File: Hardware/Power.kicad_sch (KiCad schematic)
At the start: 30 parts, among them J2 JST_2mm_LiPo, Q2 SIL2308, U10 MCP73833_MSOP, U11 AP2112K-3.3, U12 STLQ015-3.3, U4 MAX17048, U5 AP2112K-3.3

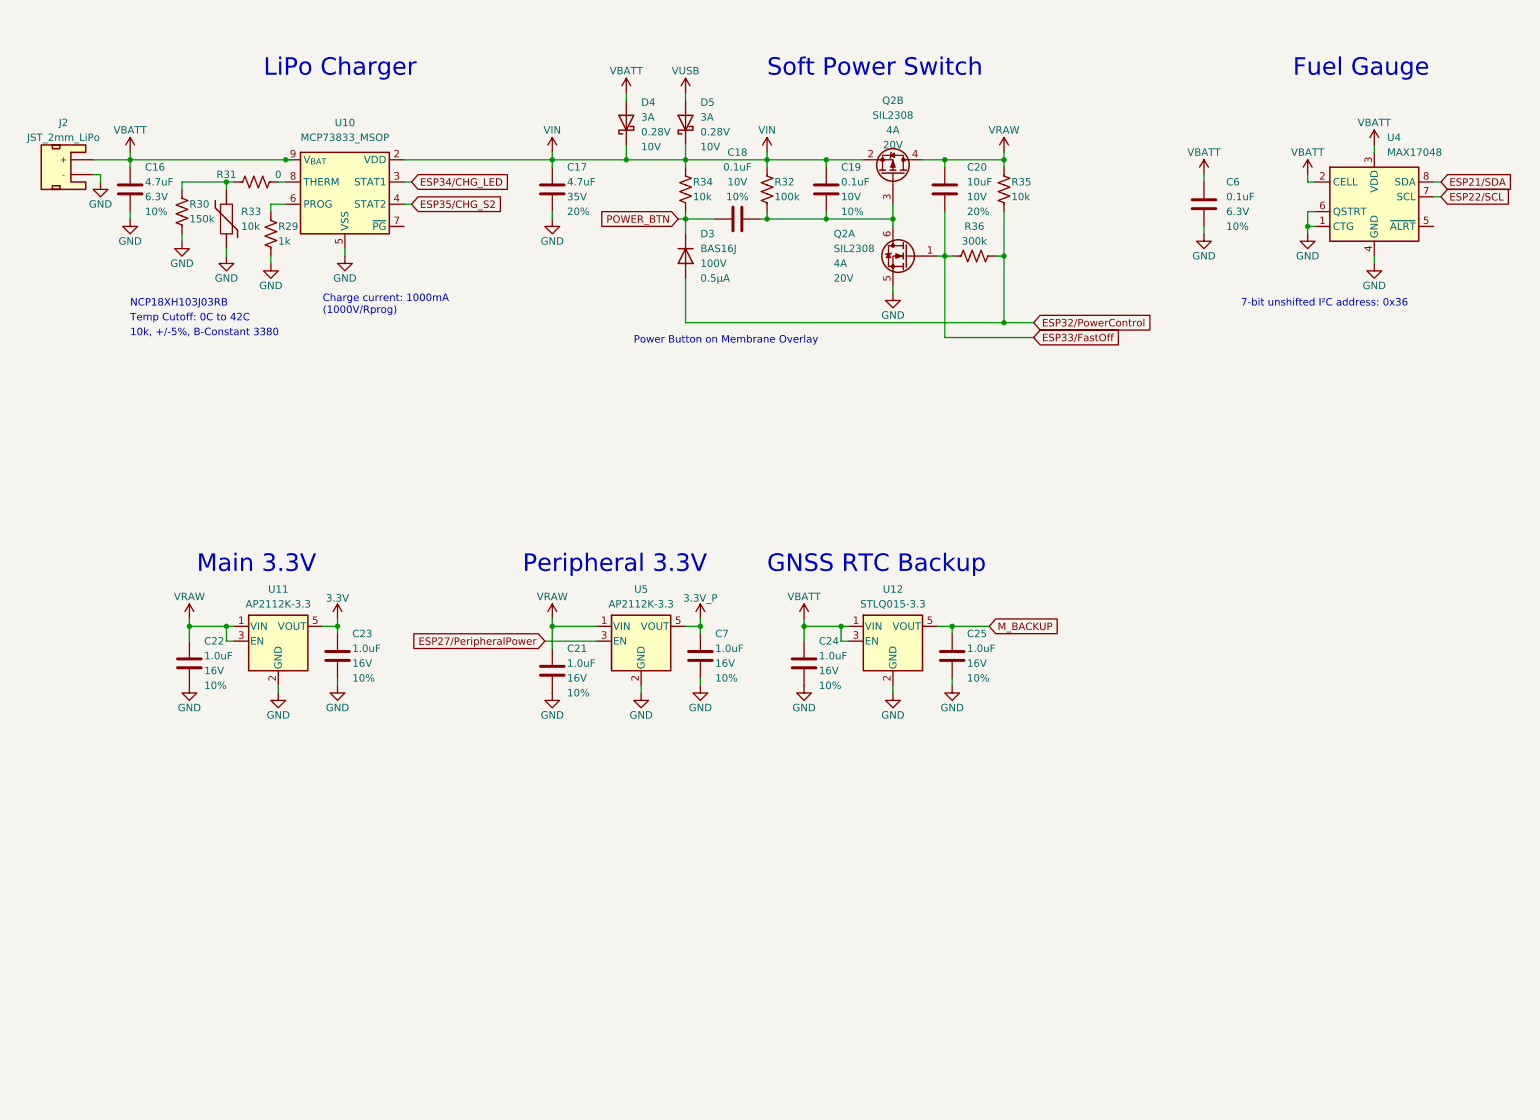
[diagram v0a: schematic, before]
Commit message: Schematic updates
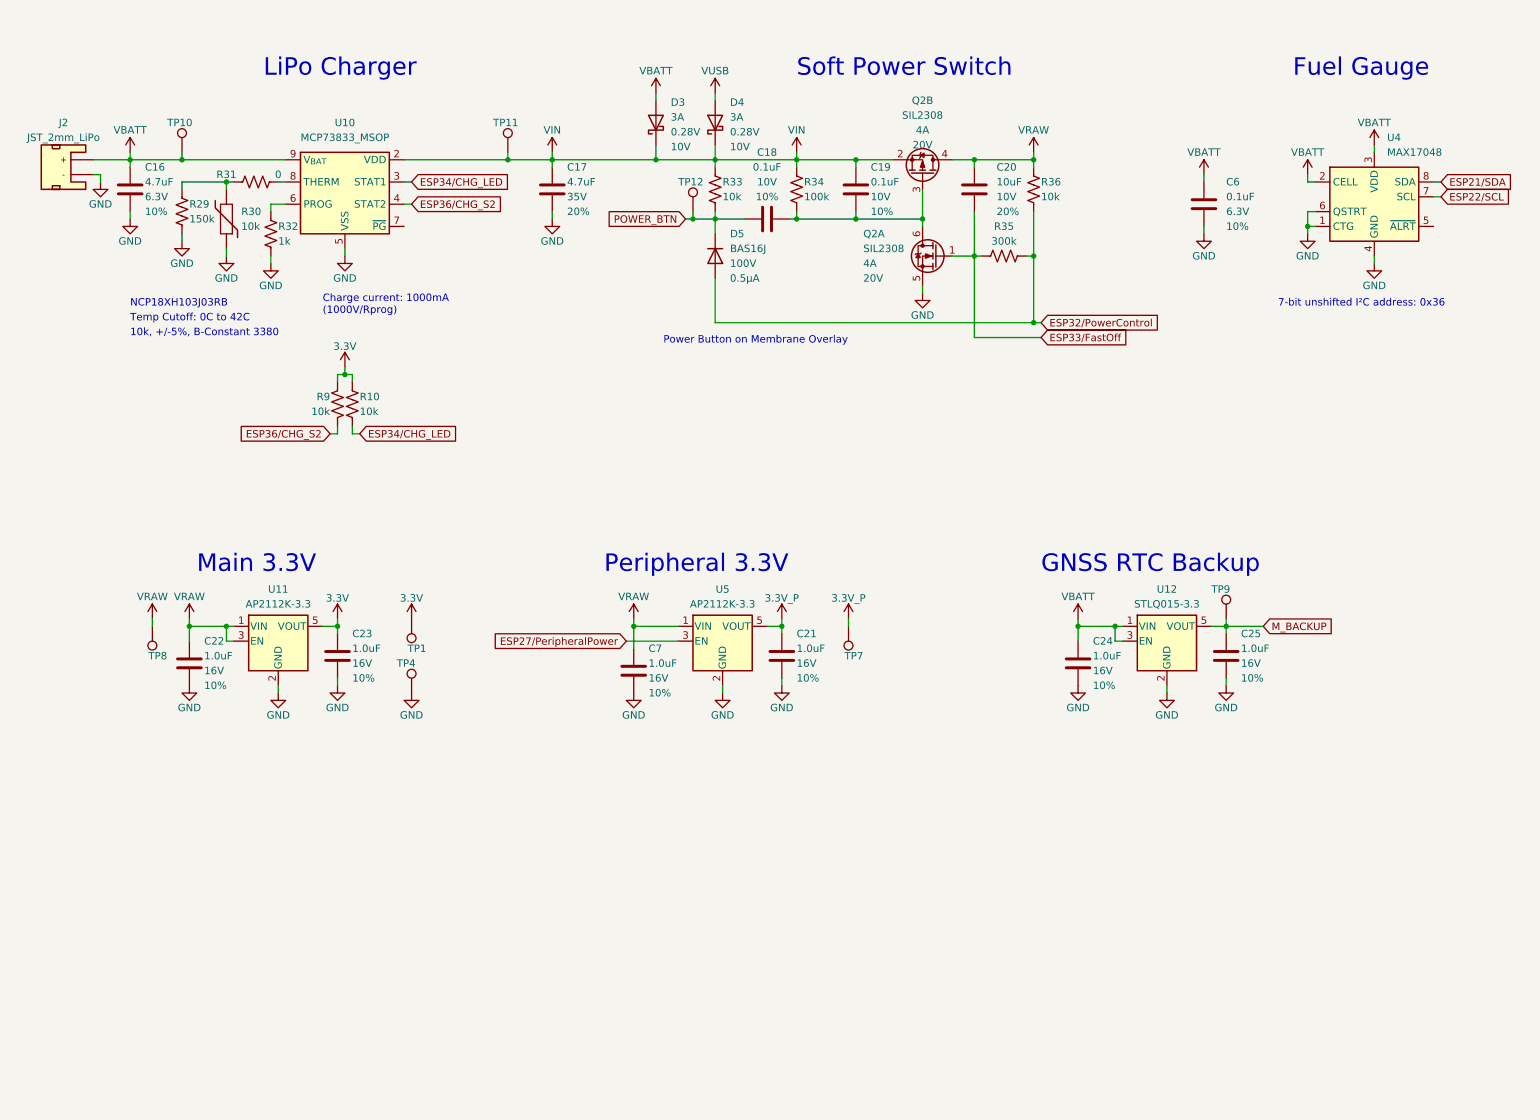
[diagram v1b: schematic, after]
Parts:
- added R10, R9: 10k, SparkFun-Resistor:R_0402_1005Metric, symbol SparkFun-Resistor:10k_0402
- added TP1, TP10, TP11, TP12, TP4, TP7, TP8, TP9: PTH, SparkFun-Connector:1X01, symbol SparkFun-Connector:TestPoint_PTH
- renumbered C7 to C21, C21 to C7, D4 to D3, D5 to D4, D3 to D5, R30 to R29, R33 to R30, R29 to R32, R34 to R33, R32 to R34, R36 to R35, R35 to R36
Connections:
- net 3.3V: now also R10.1, R9.1, TP1.1
- net 3.3V_P: now also TP7.1
- net ESP34/CHG_LED: now also R10.2
- net GND: now also U4.9 (GND), TP4.1
- net M_BACKUP: now also TP9.1
- net POWER_BTN: now also TP12.1
- net VBATT: now also TP10.1
- net VDD: now also TP11.1
- net VRAW: now also TP8.1
- net ESP35/CHG_S2 renamed ESP36/CHG_S2
- net ESP36/CHG_S2: now also R9.2
- new net: J2.NC1, J2.NC2
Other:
- moved on the sheet: C18, C19, C20, C21, C24, C25, C7, D3, D4, D5, R33, R34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

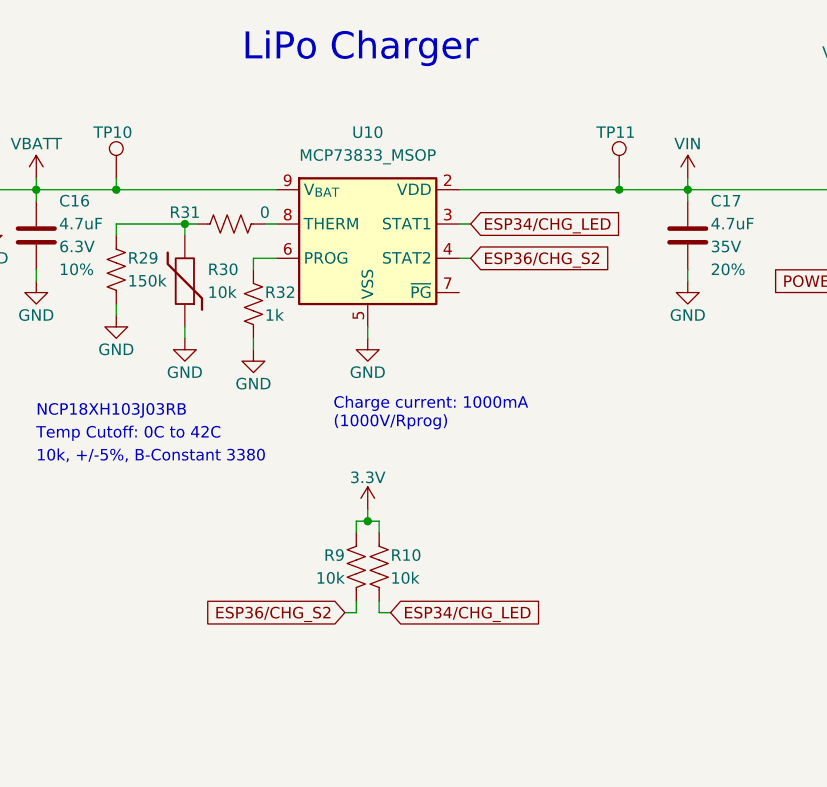
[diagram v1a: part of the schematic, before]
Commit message: Ready for airwire review
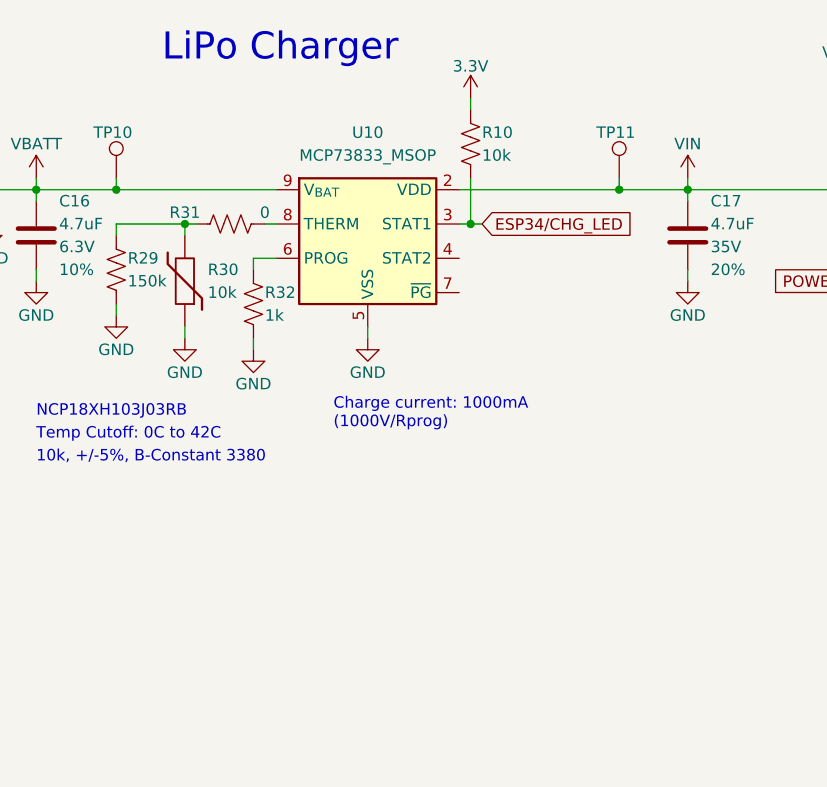
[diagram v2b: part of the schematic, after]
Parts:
- removed R9: 10k, SparkFun-Resistor:R_0402_1005Metric, symbol SparkFun-Resistor:10k_0402
- Q2: PROD_ID (none) -> TRANS-15717
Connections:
- net ESP36/CHG_S2: no longer names the net of U10.4 (STAT2)
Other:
- moved on the sheet: R10
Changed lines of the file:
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@@
   (junction (at 97.79 38.1) (diameter 0) (color 0 0 0 0)
   )
+  (junction (at 81.28 41.91) (diameter 0) (color 0 0 0 0)
+  )
   (junction (at 68.58 118.11) (diameter 0) (color 0 0 0 0)
   )
@@
   (junction (at 168.91 48.26) (diameter 0) (color 0 0 0 0)
   )
-  (junction (at 69.85 74.93) (diameter 0) (color 0 0 0 0)
-  )
   (junction (at 129.54 48.26) (diameter 0) (color 0 0 0 0)
   )
@@
     (stroke (width 0) (type default))
   )
-  (wire (pts (xy 68.58 76.2) (xy 68.58 74.93))
-    (stroke (width 0) (type default))
-  )
   (wire (pts (xy 256.54 41.91) (xy 257.81 41.91))
     (stroke (width 0) (type default))
@@
     (stroke (width 0) (type default))
   )
-  (wire (pts (xy 71.12 85.09) (xy 72.39 85.09))
-    (stroke (width 0) (type default))
-  )
   (wire (pts (xy 27.94 40.64) (xy 27.94 41.91))
     (stroke (width 0) (type default))
@@
     (stroke (width 0) (type default))
   )
+  (wire (pts (xy 81.28 41.91) (xy 82.55 41.91))
+    (stroke (width 0) (type default))
+  )
   (wire (pts (xy 66.04 118.11) (xy 68.58 118.11))
     (stroke (width 0) (type default))
@@
     (stroke (width 0) (type default))
   )
+  (wire (pts (xy 81.28 36.83) (xy 81.28 41.91))
+    (stroke (width 0) (type default))
+  )
   (wire (pts (xy 168.91 60.96) (xy 168.91 59.69))
     (stroke (width 0) (type default))
   )
-  (wire (pts (xy 68.58 83.82) (xy 68.58 85.09))
-    (stroke (width 0) (type default))
-  )
   (wire (pts (xy 43.18 118.11) (xy 43.18 120.65))
     (stroke (width 0) (type default))
@@
     (stroke (width 0) (type default))
   )
-  (wire (pts (xy 69.85 73.66) (xy 69.85 74.93))
-    (stroke (width 0) (type default))
-  )
   (wire (pts (xy 234.95 46.99) (xy 234.95 49.53))
     (stroke (width 0) (type default))
@@
     (stroke (width 0) (type default))
   )
-  (wire (pts (xy 69.85 74.93) (xy 71.12 74.93))
-    (stroke (width 0) (type default))
-  )
   (wire (pts (xy 33.02 36.83) (xy 33.02 38.1))
     (stroke (width 0) (type default))
@@
     (stroke (width 0) (type default))
   )
-  (wire (pts (xy 68.58 74.93) (xy 69.85 74.93))
-    (stroke (width 0) (type default))
-  )
   (wire (pts (xy 177.8 68.58) (xy 189.23 68.58))
     (stroke (width 0) (type default))
@@
     (stroke (width 0) (type default))
   )
-  (wire (pts (xy 68.58 85.09) (xy 67.31 85.09))
-    (stroke (width 0) (type default))
-  )
   (wire (pts (xy 146.05 48.26) (xy 147.32 48.26))
     (stroke (width 0) (type default))
@@
     (stroke (width 0) (type default))
   )
-  (wire (pts (xy 71.12 83.82) (xy 71.12 85.09))
-    (stroke (width 0) (type default))
-  )
   (wire (pts (xy 128.27 48.26) (xy 129.54 48.26))
     (stroke (width 0) (type default))
@@
     (stroke (width 0) (type default))
   )
-  (wire (pts (xy 71.12 76.2) (xy 71.12 74.93))
+  (wire (pts (xy 81.28 27.94) (xy 81.28 29.21))
     (stroke (width 0) (type default))
   )
@@
   )
   (wire (pts (xy 187.96 66.04) (xy 189.23 66.04))
-    (stroke (width 0) (type default))
-  )
-  (wire (pts (xy 80.01 45.72) (xy 81.28 45.72))
     (stroke (width 0) (type default))
   )
@@
     (effects (font (size 3 3)) (justify left bottom))
   )
-  (text "LiPo Charger" (at 55.88 24.13 0)
+  (text "LiPo Charger" (at 46.99 24.13 0)
     (effects (font (size 3 3)) (justify left bottom))
   )
@@
   (text "7-bit unshifted I²C address: 0x36\n" (at 229.87 63.5 0)
     (effects (font (size 1.27 1.27)) (justify left bottom))
-  )
-  (global_label "ESP36{slash}CHG_S2" (shape input) (at 67.31 85.09 180) (fields_autoplaced)
-    (effects (font (size 1.27 1.27)) (justify right))
-    (property "Intersheetrefs" "${INTERSHEET_REFS}" (at 49.6897 85.09 0)
-      (effects (font (size 1.27 1.27)) (justify right) hide)
-    )
   )
   (global_label "ESP21{slash}SDA" (shape input) (at 257.81 41.91 0) (fields_autoplaced)
@@
     )
   )
-  (global_label "ESP34{slash}CHG_LED" (shape input) (at 81.28 41.91 0) (fields_autoplaced)
+  (global_label "ESP34{slash}CHG_LED" (shape input) (at 82.55 41.91 0) (fields_autoplaced)
     (effects (font (size 1.27 1.27)) (justify left))
-    (property "Intersheetrefs" "${INTERSHEET_REFS}" (at 99.9284 41.91 0)
+    (property "Intersheetrefs" "${INTERSHEET_REFS}" (at 101.1984 41.91 0)
       (effects (font (size 1.27 1.27)) (justify left) hide)
     )
@@
     (effects (font (size 1.27 1.27)) (justify left))
     (property "Intersheetrefs" "${INTERSHEET_REFS}" (at 271.6808 44.45 0)
-      (effects (font (size 1.27 1.27)) (justify left) hide)
-    )
-  )
-  (global_label "ESP36{slash}CHG_S2" (shape input) (at 81.28 45.72 0) (fields_autoplaced)
-    (effects (font (size 1.27 1.27)) (justify left))
-    (property "Intersheetrefs" "${INTERSHEET_REFS}" (at 98.9003 45.72 0)
-      (effects (font (size 1.27 1.27)) (justify left) hide)
-    )
-  )
-  (global_label "ESP34{slash}CHG_LED" (shape input) (at 72.39 85.09 0) (fields_autoplaced)
-    (effects (font (size 1.27 1.27)) (justify left))
-    (property "Intersheetrefs" "${INTERSHEET_REFS}" (at 91.0384 85.09 0)
       (effects (font (size 1.27 1.27)) (justify left) hide)
     )
@@
     )
   )
-  (symbol (lib_id "SparkFun-Resistor:10k_0402") (at 68.58 80.01 270) (mirror x) (unit 1)
-    (in_bom yes) (on_board yes) (dnp no)
-    (property "Reference" "R9" (at 67.31 78.74 90)
-      (effects (font (size 1.27 1.27)) (justify right))
-    )
-    (property "Value" "10k" (at 67.31 81.28 90)
-      (effects (font (size 1.27 1.27)) (justify right))
-    )
-    (property "Footprint" "SparkFun-Resistor:R_0402_1005Metric" (at 64.516 80.01 0)
-      (effects (font (size 1.27 1.27)) hide)
-    )
-    (property "Datasheet" "https://www.vishay.com/docs/20035/dcrcwe3.pdf" (at 60.96 80.01 0)
-      (effects (font (size 1.27 1.27)) hide)
-    )
-    (property "PROD_ID" "RES-14241" (at 62.484 80.01 0)
-      (effects (font (size 1.27 1.27)) hide)
-    )
-    (pin "1")
-    (pin "2")
-    (instances
-      (project "SparkFun_RTK_Facet_mosaic"
-        (path "/e3dd3ae4-244d-4cba-9cca-5d2abf83f29a/476b4701-5340-4853-910a-2af933cad777"
-          (reference "R9") (unit 1)
-        )
-      )
-    )
-  )
   (symbol (lib_id "power:GND") (at 49.53 54.61 0) (unit 1)
     (in_bom yes) (on_board yes) (dnp no)
@@
       (effects (font (size 1.27 1.27)) hide)
     )
-    (property "PROD_ID" "~" (at 154.94 40.64 0)
+    (property "PROD_ID" "TRANS-15717" (at 154.94 40.64 0)
       (effects (font (size 1.27 1.27)) hide)
     )
@@
       (effects (font (size 1.27 1.27)) hide)
     )
-    (property "PROD_ID" "~" (at 171.45 68.58 0)
+    (property "PROD_ID" "TRANS-15717" (at 171.45 68.58 0)
       (effects (font (size 1.27 1.27)) hide)
     )
@@
     )
   )
-  (symbol (lib_id "SparkFun-PowerSymbol:3.3V") (at 69.85 73.66 0) (unit 1)
-    (in_bom yes) (on_board yes) (dnp no)
-    (property "Reference" "#PWR0112" (at 69.85 77.47 0)
-      (effects (font (size 1.27 1.27)) hide)
-    )
-    (property "Value" "3.3V" (at 69.85 70.104 0)
-      (effects (font (size 1.27 1.27)))
-    )
-    (property "Footprint" "" (at 69.85 73.66 0)
-      (effects (font (size 1.27 1.27)) hide)
-    )
-    (property "Datasheet" "" (at 69.85 73.66 0)
+  (symbol (lib_id "SparkFun-PowerSymbol:3.3V") (at 81.28 27.94 0) (unit 1)
+    (in_bom yes) (on_board yes) (dnp no)
+    (property "Reference" "#PWR0112" (at 81.28 31.75 0)
+      (effects (font (size 1.27 1.27)) hide)
+    )
+    (property "Value" "3.3V" (at 81.28 24.384 0)
+      (effects (font (size 1.27 1.27)))
+    )
+    (property "Footprint" "" (at 81.28 27.94 0)
+      (effects (font (size 1.27 1.27)) hide)
+    )
+    (property "Datasheet" "" (at 81.28 27.94 0)
       (effects (font (size 1.27 1.27)) hide)
     )
@@
     )
   )
-  (symbol (lib_id "SparkFun-Resistor:10k_0402") (at 71.12 80.01 90) (unit 1)
-    (in_bom yes) (on_board yes) (dnp no)
-    (property "Reference" "R10" (at 72.39 78.74 90)
-      (effects (font (size 1.27 1.27)) (justify right))
-    )
-    (property "Value" "10k" (at 72.39 81.28 90)
-      (effects (font (size 1.27 1.27)) (justify right))
-    )
-    (property "Footprint" "SparkFun-Resistor:R_0402_1005Metric" (at 75.184 80.01 0)
-      (effects (font (size 1.27 1.27)) hide)
-    )
-    (property "Datasheet" "https://www.vishay.com/docs/20035/dcrcwe3.pdf" (at 78.74 80.01 0)
-      (effects (font (size 1.27 1.27)) hide)
-    )
-    (property "PROD_ID" "RES-14241" (at 77.216 80.01 0)
-      (effects (font (size 1.27 1.27)) hide)
-    )
+  (symbol (lib_id "SparkFun-Resistor:10k_0402") (at 81.28 33.02 90) (unit 1)
+    (in_bom yes) (on_board yes) (dnp no)
+    (property "Reference" "R10" (at 82.55 31.75 90)
+      (effects (font (size 1.27 1.27)) (justify right))
+    )
+    (property "Value" "10k" (at 82.55 34.29 90)
+      (effects (font (size 1.27 1.27)) (justify right))
+    )
+    (property "Footprint" "SparkFun-Resistor:R_0402_1005Metric" (at 85.344 33.02 0)
+      (effects (font (size 1.27 1.27)) hide)
+    )
+    (property "Datasheet" "https://www.vishay.com/docs/20035/dcrcwe3.pdf" (at 88.9 33.02 0)
+      (effects (font (size 1.27 1.27)) hide)
+    )
+    (property "PROD_ID" "RES-14241" (at 87.376 33.02 0)
+      (effects (font (size 1.27 1.27)) hide)
+    )

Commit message: Do over with RSP32 Pico Mini - routed
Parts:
- added R9: 10k, SparkFun-Resistor:R_0402_1005Metric, symbol SparkFun-Resistor:10k_0402
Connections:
- net 3.3V: now also R9.1
- net ESP37/CHG_STAT2: now reaches U10.4 (STAT2)
- net ESP37/CHG_STAT2: now also R9.2
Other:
- moved on the sheet: C17, R10, TP11

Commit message: Switching back to the WROVER - routed
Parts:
- removed R9: 10k, SparkFun-Resistor:R_0402_1005Metric, symbol SparkFun-Resistor:10k_0402
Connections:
- net ESP37/CHG_STAT2: no longer names the net of U10.4 (STAT2)
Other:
- moved on the sheet: C17, R10, TP11

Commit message: Add extra Test Points
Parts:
- added TP23: PTH, SparkFun-Connector:1X01, symbol SparkFun-Connector:TestPoint_PTH
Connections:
- net GND: now also TP23.1
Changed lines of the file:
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@@
+    )
+  )
+  (symbol (lib_id "SparkFun-Connector:TestPoint_PTH") (at 86.36 129.54 0) (unit 1)
+    (in_bom yes) (on_board yes) (dnp no)
+    (property "Reference" "TP23" (at 83.82 124.46 0)
+      (effects (font (size 1.27 1.27)) (justify left))
+    )
+    (property "Value" "PTH" (at 86.36 133.35 0)
+      (effects (font (size 1.27 1.27)) hide)
+    )
+    (property "Footprint" "SparkFun-Connector:1X01" (at 85.09 135.89 0)
+      (effects (font (size 1.27 1.27)) hide)
+    )
+    (property "Datasheet" "~" (at 86.36 137.16 0)
+      (effects (font (size 1.27 1.27)) hide)
+    )
+    (pin "1")
+    (instances
+      (project "SparkFun_RTK_Facet_mosaic"
+        (path "/e3dd3ae4-244d-4cba-9cca-5d2abf83f29a/476b4701-5340-4853-910a-2af933cad777"
+          (reference "TP23") (unit 1)
+        )
+      )
     )
   )
@@
         )
       )
+    )
+  )
+  (symbol (lib_id "SparkFun-PowerSymbol:GND") (at 86.36 129.54 0) (unit 1)
+    (in_bom yes) (on_board yes) (dnp no)
+    (property "Reference" "#PWR0118" (at 86.36 135.89 0)
+      (effects (font (size 1.27 1.27)) hide)
+    )
+    (property "Value" "GND" (at 86.36 133.35 0)
+      (effects (font (size 1.27 1.27)))
+    )
+    (property "Footprint" "" (at 86.36 129.54 0)
+      (effects (font (size 1.27 1.27)) hide)
+    )
+    (property "Datasheet" "" (at 86.36 129.54 0)
+      (effects (font (size 1.27 1.27)) hide)
+    )
+    (pin "1")
+    (instances
+      (project "SparkFun_RTK_Facet_mosaic"
+        (path "/e3dd3ae4-244d-4cba-9cca-5d2abf83f29a/476b4701-5340-4853-910a-2af933cad777"
+          (reference "#PWR0118") (unit 1)
+        )
+      )
